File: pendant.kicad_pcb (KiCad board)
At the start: 2 copper layers, 29.2 x 74.9 mm, 3 parts, among them J1 AudioJack4_Ground, J2 AudioJack4_Ground, U1 BlackPillSymple

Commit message: Updaet PCB design
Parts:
- added R1: 2.2 k, Resistor_SMD:R_0603_1608Metric, F.Cu at (130.8, 63.5)
- added R2: 2.2 k, Resistor_SMD:R_0603_1608Metric, F.Cu at (134.6, 63.5)
- added R3: 2.2 k, Resistor_SMD:R_0603_1608Metric, F.Cu at (130.8, 68.6)
- added R4: 2.2 k, Resistor_SMD:R_0603_1608Metric, F.Cu at (134.6, 68.6)
- J1, J2: value AudioJack4_Ground -> AudioJack4
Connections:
- J1 pad R1: SDA1 -> SCL1
- J1 pad R2: SCL1 -> SDA1
- J2 pad R1: SDA2 -> SCL2
- J2 pad R2: SCL2 -> SDA2
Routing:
- net 3V3: track 71.2 -> 87.8 mm, vias 0 -> 2
- net SDA1: track 55.3 -> 68.4 mm, vias 0 -> 1
- net SDA2: track 24.1 -> 35.5 mm
- net SCL1: track 57.4 -> 60.8 mm
- net SCL2: track 31.2 -> 33.9 mm
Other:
- board size 29.2 x 74.9 mm -> 31.8 x 74.9 mm

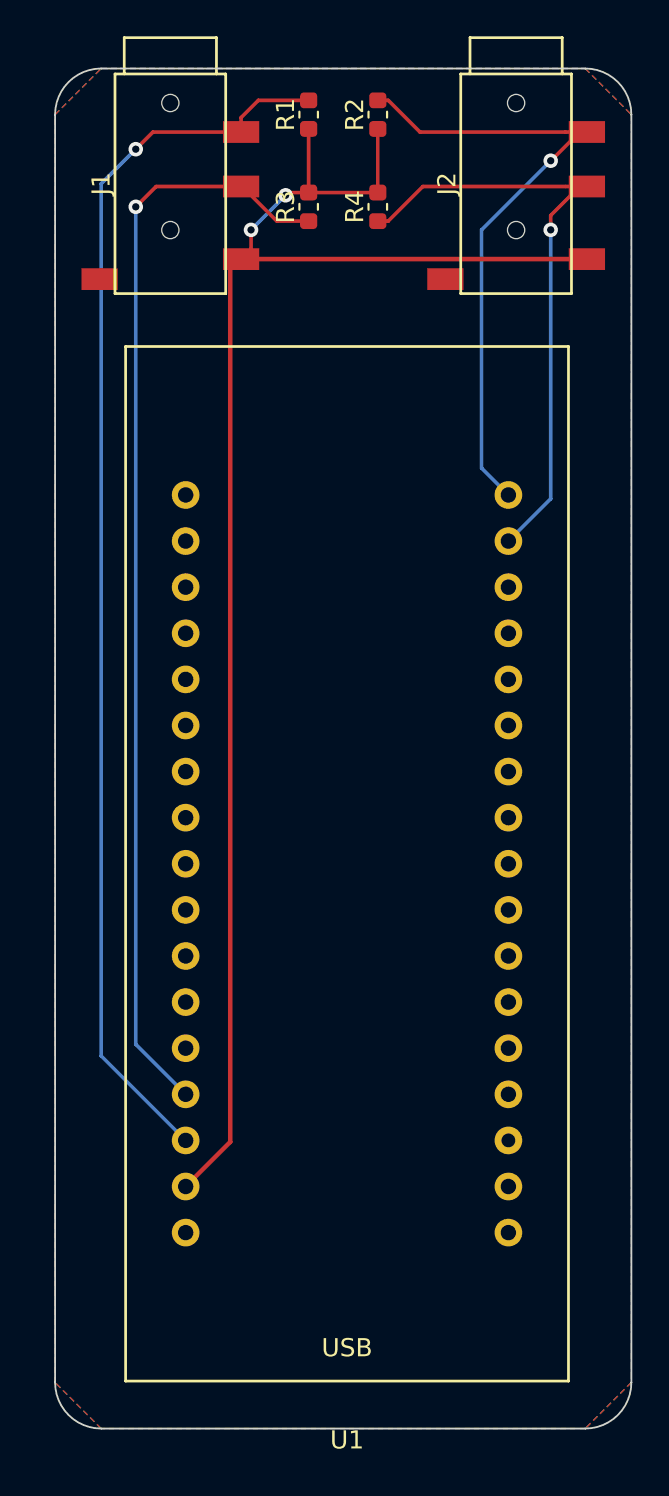
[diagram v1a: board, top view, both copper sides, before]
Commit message: Fix power line width
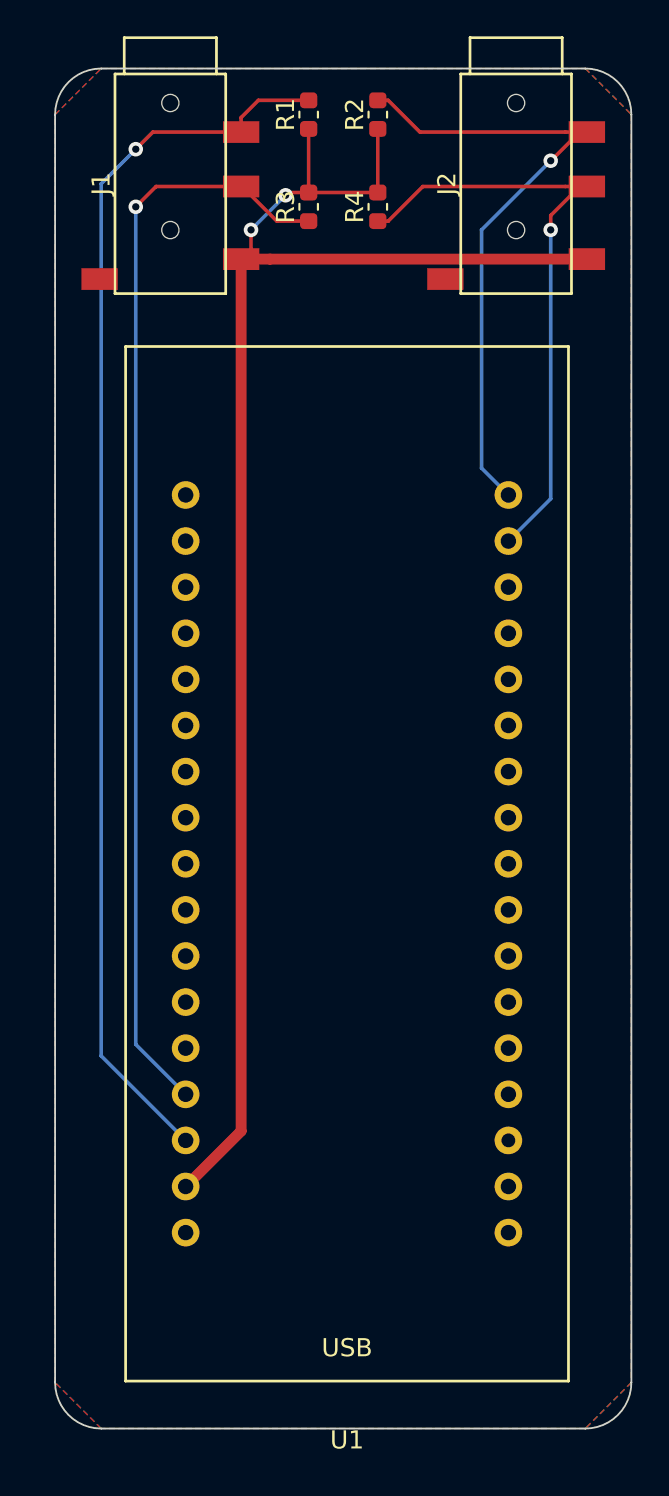
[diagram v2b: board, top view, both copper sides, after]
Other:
- net class Power added: clearance 0.2, trace_width 0.6, via_dia 0.8, via_drill 0.4
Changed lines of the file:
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@@
     (thickness 1.6)
     (drawings 8)
-    (tracks 51)
+    (tracks 52)
     (zones 0)
     (modules 7)
@@
     (uvia_dia 0.3)
     (uvia_drill 0.1)
-    (add_net 3V3)
-    (add_net GND)
     (add_net "Net-(U1-Pad1)")
     (add_net "Net-(U1-Pad10)")
@@
     (add_net SDA2)
   )
-  (module library:TRRS_SMD_PJ320 (layer F.Cu)
-    (at 123.19 67.31 270)
-    (fp_text reference J1 (at 0 3.81 270) (layer F.SilkS)
-      (effects (font (size 1 1) (thickness 0.15)))
-    )
-    (fp_text value AudioJack4 (at 0 6.35 270) (layer F.Fab)
-      (effects (font (size 1 1) (thickness 0.15)))
-    )
-    (fp_line (start -8.05 2.54) (end -6.05 2.54) (layer F.SilkS) (width 0.15))
-    (fp_line (start -8.05 -2.54) (end -8.05 2.54) (layer F.SilkS) (width 0.15))
-    (fp_line (start -6.05 -2.54) (end -8.05 -2.54) (layer F.SilkS) (width 0.15))
-    (fp_line (start -6.05 3.05) (end -6.05 -3.05) (layer F.SilkS) (width 0.15))
-    (fp_line (start 6.05 3.05) (end -6.05 3.05) (layer F.SilkS) (width 0.15))
-    (fp_line (start 6.05 -3.05) (end 6.05 3.05) (layer F.SilkS) (width 0.15))
-    (fp_line (start -6.05 -3.05) (end 6.05 -3.05) (layer F.SilkS) (width 0.15))
-    (pad R2 smd rect (at -2.85 -3.9 270) (size 1.2 2) (layers F.Cu F.Paste F.Mask)
-      (net 3 SDA1))
-    (pad R1 smd rect (at 0.15 -3.9 270) (size 1.2 2) (layers F.Cu F.Paste F.Mask)
-      (net 4 SCL1))
-    (pad T smd rect (at 4.15 -3.9 270) (size 1.2 2) (layers F.Cu F.Paste F.Mask)
-      (net 2 3V3))
-    (pad S smd rect (at 5.25 3.9 270) (size 1.2 2) (layers F.Cu F.Paste F.Mask)
-      (net 1 GND))
-    (pad "" np_thru_hole circle (at 2.55 0 270) (size 0.95 0.95) (drill 0.95) (layers *.Cu *.Mask))
-    (pad "" np_thru_hole circle (at -4.45 0 270) (size 0.95 0.95) (drill 0.95) (layers *.Cu *.Mask))
-  )
-  (module library:TRRS_SMD_PJ320 (layer F.Cu)
-    (at 142.24 67.31 270)
-    (fp_text reference J2 (at 0 3.81 270) (layer F.SilkS)
-      (effects (font (size 1 1) (thickness 0.15)))
-    )
-    (fp_text value AudioJack4 (at 0 -6.35 270) (layer F.Fab)
-      (effects (font (size 1 1) (thickness 0.15)))
-    )
-    (fp_line (start -8.05 2.54) (end -6.05 2.54) (layer F.SilkS) (width 0.15))
-    (fp_line (start -8.05 -2.54) (end -8.05 2.54) (layer F.SilkS) (width 0.15))
-    (fp_line (start -6.05 -2.54) (end -8.05 -2.54) (layer F.SilkS) (width 0.15))
-    (fp_line (start -6.05 3.05) (end -6.05 -3.05) (layer F.SilkS) (width 0.15))
-    (fp_line (start 6.05 3.05) (end -6.05 3.05) (layer F.SilkS) (width 0.15))
-    (fp_line (start 6.05 -3.05) (end 6.05 3.05) (layer F.SilkS) (width 0.15))
-    (fp_line (start -6.05 -3.05) (end 6.05 -3.05) (layer F.SilkS) (width 0.15))
-    (pad R2 smd rect (at -2.85 -3.9 270) (size 1.2 2) (layers F.Cu F.Paste F.Mask)
-      (net 6 SDA2))
-    (pad R1 smd rect (at 0.15 -3.9 270) (size 1.2 2) (layers F.Cu F.Paste F.Mask)
-      (net 5 SCL2))
-    (pad T smd rect (at 4.15 -3.9 270) (size 1.2 2) (layers F.Cu F.Paste F.Mask)
-      (net 2 3V3))
-    (pad S smd rect (at 5.25 3.9 270) (size 1.2 2) (layers F.Cu F.Paste F.Mask)
-      (net 1 GND))
-    (pad "" np_thru_hole circle (at 2.55 0 270) (size 0.95 0.95) (drill 0.95) (layers *.Cu *.Mask))
-    (pad "" np_thru_hole circle (at -4.45 0 270) (size 0.95 0.95) (drill 0.95) (layers *.Cu *.Mask))
+  (net_class Power ""
+    (clearance 0.2)
+    (trace_width 0.6)
+    (via_dia 0.8)
+    (via_drill 0.4)
+    (uvia_dia 0.3)
+    (uvia_drill 0.1)
+    (add_net 3V3)
+    (add_net GND)
   )
   (module library:BlackPillSimple (layer F.Cu)
@@
       (net 6 SDA2))
   )
+  (module library:TRRS_SMD_PJ320 (layer F.Cu)
+    (at 123.19 67.31 270)
+    (fp_text reference J1 (at 0 3.81 270) (layer F.SilkS)
+      (effects (font (size 1 1) (thickness 0.15)))
+    )
+    (fp_text value AudioJack4 (at 0 6.35 270) (layer F.Fab)
+      (effects (font (size 1 1) (thickness 0.15)))
+    )
+    (fp_line (start -8.05 2.54) (end -6.05 2.54) (layer F.SilkS) (width 0.15))
+    (fp_line (start -8.05 -2.54) (end -8.05 2.54) (layer F.SilkS) (width 0.15))
+    (fp_line (start -6.05 -2.54) (end -8.05 -2.54) (layer F.SilkS) (width 0.15))
+    (fp_line (start -6.05 3.05) (end -6.05 -3.05) (layer F.SilkS) (width 0.15))
+    (fp_line (start 6.05 3.05) (end -6.05 3.05) (layer F.SilkS) (width 0.15))
+    (fp_line (start 6.05 -3.05) (end 6.05 3.05) (layer F.SilkS) (width 0.15))
+    (fp_line (start -6.05 -3.05) (end 6.05 -3.05) (layer F.SilkS) (width 0.15))
+    (pad R2 smd rect (at -2.85 -3.9 270) (size 1.2 2) (layers F.Cu F.Paste F.Mask)
+      (net 3 SDA1))
+    (pad R1 smd rect (at 0.15 -3.9 270) (size 1.2 2) (layers F.Cu F.Paste F.Mask)
+      (net 4 SCL1))
+    (pad T smd rect (at 4.15 -3.9 270) (size 1.2 2) (layers F.Cu F.Paste F.Mask)
+      (net 2 3V3))
+    (pad S smd rect (at 5.25 3.9 270) (size 1.2 2) (layers F.Cu F.Paste F.Mask)
+      (net 1 GND))
+    (pad "" np_thru_hole circle (at 2.55 0 270) (size 0.95 0.95) (drill 0.95) (layers *.Cu *.Mask))
+    (pad "" np_thru_hole circle (at -4.45 0 270) (size 0.95 0.95) (drill 0.95) (layers *.Cu *.Mask))
+  )
+  (module library:TRRS_SMD_PJ320 (layer F.Cu)
+    (at 142.24 67.31 270)
+    (fp_text reference J2 (at 0 3.81 270) (layer F.SilkS)
+      (effects (font (size 1 1) (thickness 0.15)))
+    )
+    (fp_text value AudioJack4 (at 0 -6.35 270) (layer F.Fab)
+      (effects (font (size 1 1) (thickness 0.15)))
+    )
+    (fp_line (start -8.05 2.54) (end -6.05 2.54) (layer F.SilkS) (width 0.15))
+    (fp_line (start -8.05 -2.54) (end -8.05 2.54) (layer F.SilkS) (width 0.15))
+    (fp_line (start -6.05 -2.54) (end -8.05 -2.54) (layer F.SilkS) (width 0.15))
+    (fp_line (start -6.05 3.05) (end -6.05 -3.05) (layer F.SilkS) (width 0.15))
+    (fp_line (start 6.05 3.05) (end -6.05 3.05) (layer F.SilkS) (width 0.15))
+    (fp_line (start 6.05 -3.05) (end 6.05 3.05) (layer F.SilkS) (width 0.15))
+    (fp_line (start -6.05 -3.05) (end 6.05 -3.05) (layer F.SilkS) (width 0.15))
+    (pad R2 smd rect (at -2.85 -3.9 270) (size 1.2 2) (layers F.Cu F.Paste F.Mask)
+      (net 6 SDA2))
+    (pad R1 smd rect (at 0.15 -3.9 270) (size 1.2 2) (layers F.Cu F.Paste F.Mask)
+      (net 5 SCL2))
+    (pad T smd rect (at 4.15 -3.9 270) (size 1.2 2) (layers F.Cu F.Paste F.Mask)
+      (net 2 3V3))
+    (pad S smd rect (at 5.25 3.9 270) (size 1.2 2) (layers F.Cu F.Paste F.Mask)
+      (net 1 GND))
+    (pad "" np_thru_hole circle (at 2.55 0 270) (size 0.95 0.95) (drill 0.95) (layers *.Cu *.Mask))
+    (pad "" np_thru_hole circle (at -4.45 0 270) (size 0.95 0.95) (drill 0.95) (layers *.Cu *.Mask))
+  )
   (module Resistor_SMD:R_0603_1608Metric (layer F.Cu)
     (at 130.81 63.5 90)
@@
   (gr_line (start 148.59 133.35) (end 148.59 63.5) (layer Edge.Cuts) (width 0.1))
   (gr_line (start 116.84 63.5) (end 116.84 133.35) (layer Edge.Cuts) (width 0.1))
-  (segment (start 145.54 71.46) (end 126.49 71.46) (width 0.25) (layer F.Cu) (net 2))
-  (segment (start 126.49 120.100002) (end 124.035001 122.555001) (width 0.25) (layer F.Cu) (net 2))
-  (segment (start 126.49 71.46) (end 126.49 120.100002) (width 0.25) (layer F.Cu) (net 2))
   (segment (start 130.81 64.2875) (end 130.81 67.7925) (width 0.2) (layer F.Cu) (net 2))
   (segment (start 134.62 64.2875) (end 134.62 67.7925) (width 0.2) (layer F.Cu) (net 2))
@@
   (segment (start 127.635 70.915) (end 127.09 71.46) (width 0.2) (layer F.Cu) (net 2))
   (segment (start 127.635 69.85) (end 127.635 70.915) (width 0.2) (layer F.Cu) (net 2))
+  (segment (start 127.09 119.500002) (end 124.035001 122.555001) (width 0.6) (layer F.Cu) (net 2))
+  (segment (start 127.09 71.46) (end 127.09 119.500002) (width 0.6) (layer F.Cu) (net 2))
+  (segment (start 128.69 71.46) (end 146.14 71.46) (width 0.6) (layer F.Cu) (net 2))
+  (segment (start 127.09 71.46) (end 128.69 71.46) (width 0.6) (layer F.Cu) (net 2))
   (segment (start 127.09 63.66) (end 127.09 64.46) (width 0.2) (layer F.Cu) (net 3))
   (segment (start 128.0375 62.7125) (end 127.09 63.66) (width 0.2) (layer F.Cu) (net 3))
